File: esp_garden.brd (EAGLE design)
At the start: 50 x 100 mm, 33 parts, among them IC1 REG1117, T1 DMN6068SE-13, T2 DMN6068SE-13, T3 DMN6068SE-13, T4 DMN6068SE-13, U1 V1, U10 V1, U11 V1, U12 V1, U14 V1, U15 V1, U2 V1, U3 V1, U4 V1, U5 V1, U6 V1, U7 V1, U8 V1, U9 V1

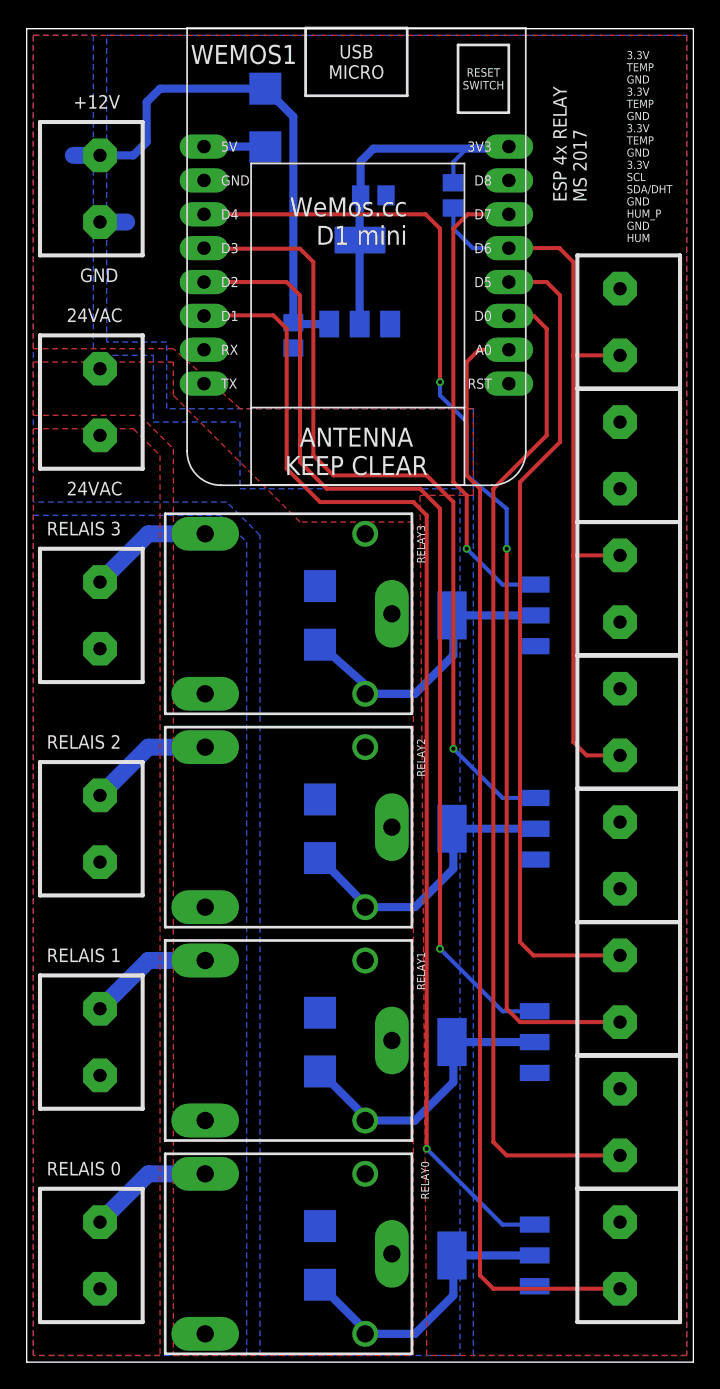
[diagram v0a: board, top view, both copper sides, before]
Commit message: added options for DHT22 onboard and special use for relais 0
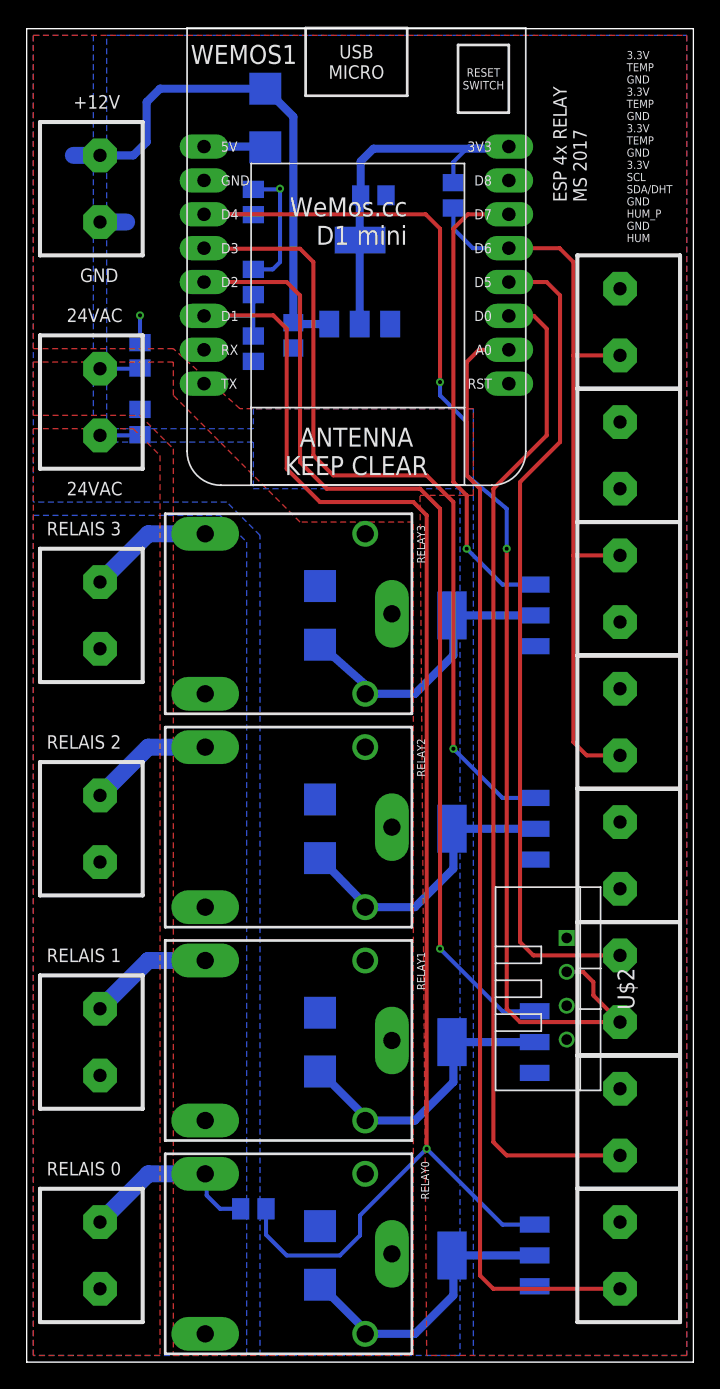
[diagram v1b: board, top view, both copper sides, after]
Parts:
- added R2: 4.7k, rcl:M0805
- added R3, R4, R5, R6, R7: n.a., rcl:M0805
- added U$2: TEMP-HUM-SENSOR-DHT22, diy-modules:TEMP-HUM-SENSOR-DHT22
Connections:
- net +3V3: now also R2.2, R4.1, R6.1, U$2.1
- net +UB: now also R6.2
- net -UB: now also R7.2
- net GND: now also R5.2, R7.1, U$2.4
- net N$4: now also R3.1
- net RELAY_0: now also R3.2, R4.2, R5.1
- net SDA/DHT: now also R2.1, U$2.2
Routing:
- net RELAY_0: track 87.0 -> 112.7 mm
- net +3V3: track 30.0 -> 42.0 mm, vias 0 -> 2
- net SDA/DHT: track 87.8 -> 97.7 mm
- net N$4: track 9.39 -> 14.0 mm
- net -UB: track 0.00 -> 3.02 mm
- net +UB: track 0.00 -> 3.02 mm
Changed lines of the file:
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@@
 </element>
 <element name="U$1" library="JKW_CHIP" package="LOGO_ROHS_NO_TRASH" value="LOGO_NO_TRASHNO_TRASH" x="47.5" y="91.5" rot="MR0"/>
+<element name="U$2" library="diy-modules" package="TEMP-HUM-SENSOR-DHT22" value="TEMP-HUM-SENSOR-DHT22" x="40.5" y="28" rot="R270"/>
+<element name="R2" library="rcl" package="M0805" value="4.7k" x="17" y="87" rot="MR90"/>
+<element name="R3" library="rcl" package="M0805" value="n.a." x="17" y="11.5" rot="MR180"/>
+<element name="R4" library="rcl" package="M0805" value="n.a." x="17" y="81" rot="MR270"/>
+<element name="R5" library="rcl" package="M0805" value="n.a." x="17" y="76" rot="MR270"/>
+<element name="R6" library="rcl" package="M0805" value="n.a." x="8.5" y="75.5" rot="MR270"/>
+<element name="R7" library="rcl" package="M0805" value="n.a." x="8.5" y="70.5" rot="MR270"/>
 </elements>
 <signals>
@@
 <vertex x="33.5" y="0.5"/>
 <vertex x="33.5" y="71.5"/>
-<vertex x="10.5" y="71.5"/>
-<vertex x="10.5" y="76.5"/>
-<vertex x="6" y="76.5"/>
+<vertex x="17" y="71.5"/>
+<vertex x="17" y="70"/>
+<vertex x="6" y="70"/>
 </polygon>
 <wire x1="5.5" y1="85.5" x2="7.5" y2="85.5" width="1.27" layer="16"/>
@@
 <contactref element="C1" pad="2"/>
 <contactref element="C2" pad="2"/>
+<contactref element="U$2" pad="4"/>
+<contactref element="R7" pad="1"/>
+<contactref element="R5" pad="2"/>
 </signal>
 <signal name="RELAY_L_3">
@@
 <vertex x="0.5" y="99.5"/>
 <vertex x="5" y="99.5"/>
-<vertex x="5" y="75.5"/>
-<vertex x="9.5" y="75.5"/>
-<vertex x="9.5" y="70.5"/>
-<vertex x="16" y="70.5"/>
-<vertex x="16" y="65.5"/>
+<vertex x="5" y="69"/>
+<vertex x="17" y="69"/>
+<vertex x="17" y="65.5"/>
 <vertex x="32.5" y="65.5"/>
 <vertex x="32.5" y="0.5"/>
@@
 <wire x1="26" y1="91" x2="36" y2="91" width="0.6096" layer="16"/>
 <wire x1="36" y1="91" x2="36.16" y2="91.16" width="0.6096" layer="16"/>
+<contactref element="U$2" pad="1"/>
+<contactref element="R2" pad="2"/>
+<wire x1="19" y1="87.95" x2="17" y2="87.95" width="0.3048" layer="16"/>
+<wire x1="19" y1="87.95" x2="19" y2="88" width="0.3048" layer="16"/>
+<via x="19" y="88" extent="1-16" drill="0.3048"/>
+<contactref element="R6" pad="1"/>
+<wire x1="8.5" y1="76.45" x2="8.5" y2="78.5" width="0.3048" layer="16"/>
+<via x="8.5" y="78.5" extent="1-16" drill="0.3048"/>
+<wire x1="36.32" y1="91" x2="36.16" y2="91.16" width="0.3048" layer="16"/>
+<contactref element="R4" pad="1"/>
+<wire x1="17" y1="81.95" x2="18.45" y2="81.95" width="0.3048" layer="16"/>
+<wire x1="18.45" y1="81.95" x2="19" y2="82.5" width="0.3048" layer="16"/>
+<wire x1="19" y1="82.5" x2="19" y2="87.95" width="0.3048" layer="16"/>
 </signal>
 <signal name="RELAY_0">
@@
 <contactref element="WEMOS1" pad="D1"/>
 <wire x1="38.099" y1="10.311" x2="35.689" y2="10.311" width="0.3048" layer="16"/>
-<wire x1="35.689" y1="10.311" x2="30" y2="16" width="0.3048" layer="16"/>
+<wire x1="30" y1="16" x2="35.689" y2="10.311" width="0.3048" layer="16"/>
 <via x="30" y="16" extent="1-16" drill="0.3048"/>
 <wire x1="30" y1="16" x2="30" y2="63.5" width="0.3048" layer="1"/>
@@
 <wire x1="18.5" y1="78.5" x2="13.34" y2="78.5" width="0.3048" layer="1"/>
 <wire x1="13.34" y1="78.5" x2="13.3" y2="78.46" width="0.3048" layer="1"/>
+<contactref element="R3" pad="2"/>
+<contactref element="R5" pad="1"/>
+<contactref element="R4" pad="2"/>
+<wire x1="16.96" y1="78.46" x2="13.3" y2="78.46" width="0.3048" layer="16"/>
+<wire x1="16.96" y1="78.46" x2="17" y2="78.5" width="0.3048" layer="16"/>
+<wire x1="17" y1="78.5" x2="17" y2="80.05" width="0.3048" layer="16"/>
+<wire x1="17" y1="76.95" x2="17" y2="78.42" width="0.3048" layer="16"/>
+<wire x1="17" y1="78.42" x2="16.96" y2="78.46" width="0.3048" layer="16"/>
+<wire x1="17.95" y1="11.5" x2="17.95" y2="9.55" width="0.3048" layer="16"/>
+<wire x1="17.95" y1="9.55" x2="19.5" y2="8" width="0.3048" layer="16"/>
+<wire x1="19.5" y1="8" x2="23.5" y2="8" width="0.3048" layer="16"/>
+<wire x1="23.5" y1="8" x2="25" y2="9.5" width="0.3048" layer="16"/>
+<wire x1="25" y1="9.5" x2="25" y2="11" width="0.3048" layer="16"/>
+<wire x1="25" y1="11" x2="30" y2="16" width="0.3048" layer="16"/>
 </signal>
 <signal name="RELAY_1">
@@
 <vertex x="0.5" y="75"/>
 </polygon>
+<contactref element="R6" pad="2"/>
+<wire x1="5.5" y1="74.5" x2="8.45" y2="74.5" width="0.3048" layer="16"/>
+<wire x1="8.45" y1="74.5" x2="8.5" y2="74.55" width="0.3048" layer="16"/>
 </signal>
 <signal name="-UB">
@@
 <vertex x="0.5" y="0.5"/>
 </polygon>
+<contactref element="R7" pad="2"/>
+<wire x1="5.5" y1="69.5" x2="8.45" y2="69.5" width="0.3048" layer="16"/>
+<wire x1="8.45" y1="69.5" x2="8.5" y2="69.55" width="0.3048" layer="16"/>
 </signal>
 <signal name="N$4">
@@
 <wire x1="5.5" y1="10.5" x2="9.12" y2="14.12" width="1.27" layer="16"/>
 <contactref element="RELAY0" pad="SWOPEN"/>
-<wire x1="9.12" y1="14.12" x2="13.39" y2="14.12" width="1.27" layer="16"/>
+<wire x1="13.39" y1="14.12" x2="9.12" y2="14.12" width="1.27" layer="16"/>
+<contactref element="R3" pad="1"/>
+<wire x1="16.05" y1="11.5" x2="14.5" y2="11.5" width="0.3048" layer="16"/>
+<wire x1="14.5" y1="11.5" x2="13.5" y2="12.5" width="0.3048" layer="16"/>
+<wire x1="13.5" y1="12.5" x2="13.5" y2="14.01" width="0.3048" layer="16"/>
+<wire x1="13.5" y1="14.01" x2="13.39" y2="14.12" width="0.3048" layer="16"/>
 </signal>
 <signal name="N$6">
@@
 <wire x1="33" y1="66.5" x2="36" y2="64" width="0.3048" layer="16"/>
 <wire x1="36" y1="64" x2="36" y2="61" width="0.3048" layer="16"/>
+<contactref element="U$2" pad="2"/>
+<contactref element="R2" pad="1"/>
+<wire x1="13.3" y1="86.08" x2="17" y2="86.08" width="0.3048" layer="16"/>
+<wire x1="17" y1="86.08" x2="17" y2="86.05" width="0.3048" layer="16"/>
+<wire x1="40.5" y1="29.27" x2="41.73" y2="29.27" width="0.3048" layer="1"/>
+<wire x1="41.73" y1="29.27" x2="42.5" y2="28.5" width="0.3048" layer="1"/>
+<wire x1="42.5" y1="28.5" x2="42.5" y2="27.5" width="0.3048" layer="1"/>
+<wire x1="42.5" y1="27.5" x2="44.5" y2="25.5" width="0.3048" layer="1"/>
 </signal>
 <signal name="SCL">

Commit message: added rectifier
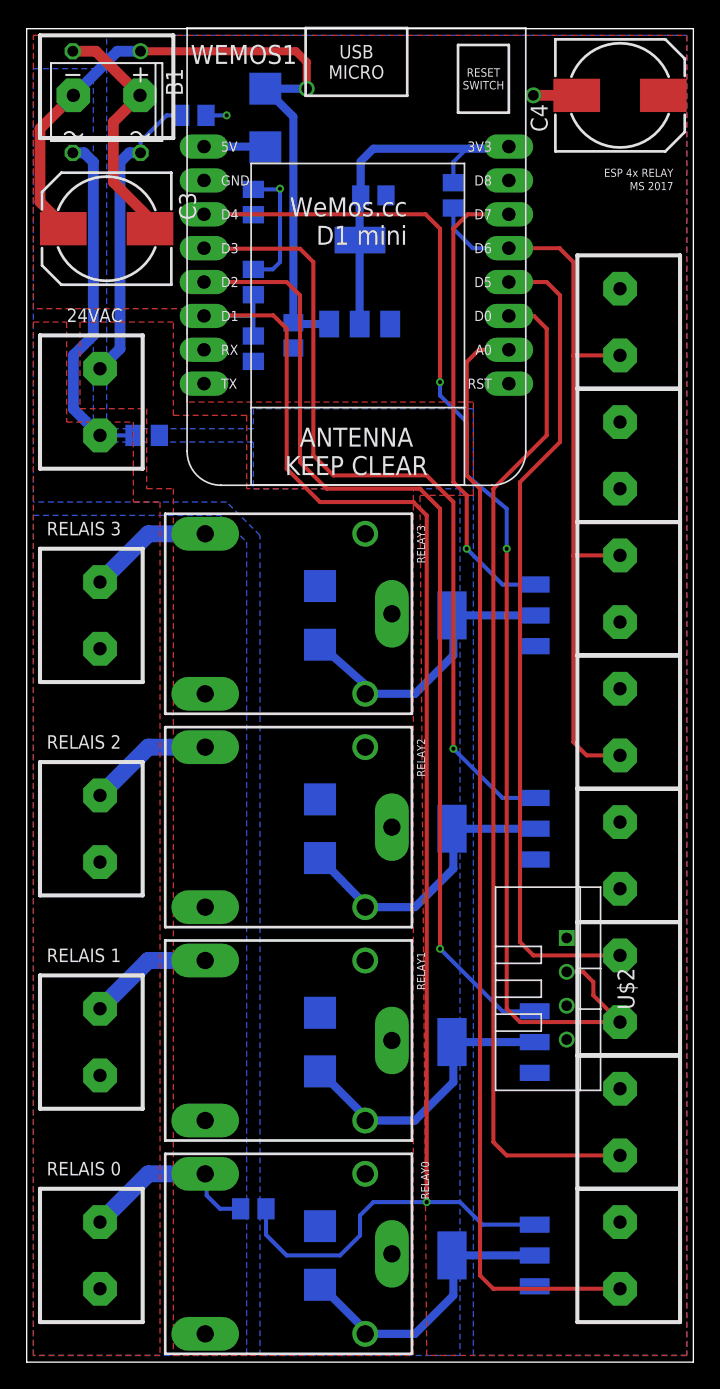
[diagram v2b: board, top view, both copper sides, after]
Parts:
- added B1: DBL202G, rectifier:DB
- added C3, C4: (no value), rcl:150CLZ-0810
- RELAY0, RELAY1, RELAY2, RELAY3: value SRD-05VDC-SL-C -> SRD-30VDC-SL-C
- moved R6 18.4 mm to (12.5, 93.5), turned to 0 degrees
- moved U5 7.57 mm to (6.00, 95.5), turned to 180 degrees
- moved R7 1.12 mm to (9.00, 69.5), turned to 0 degrees
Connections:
- net +12V: now also B1.+, C3.+, U5.P$2; no longer U5.P$1
- net +3V3: now also C4.+
- net +UB: now also B1.AC2
- net -UB: now also B1.AC1
- net GND: now also B1.-, C3.-, C4.-, U5.P$1; no longer U5.P$2
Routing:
- net -UB: track 3.02 -> 26.3 mm
- net GND: track 2.00 -> 21.6 mm, vias 0 -> 1
- net +UB: track 3.02 -> 22.6 mm
- net +12V: track 42.1 -> 57.2 mm, vias 0 -> 1
- net RELAY_0: track 112.7 -> 113.3 mm
- net +3V3: track 42.0 -> 41.5 mm
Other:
- board text removed: "3.3V TEMP GND 3.3V TEMP GND 3.3V TEMP GND 3.3V SCL SDA/DHT GND HUM_P GND HUM"
